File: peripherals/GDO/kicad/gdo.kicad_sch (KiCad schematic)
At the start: 11 parts, among them J1 Conn_01x15_Pin, J2 Conn_01x02_Pin, J4 Conn_01x03_Pin, J5 Conn_01x03_Pin, J6 Conn_01x03_Pin, Q1 2N7002, Q2 AO3400A

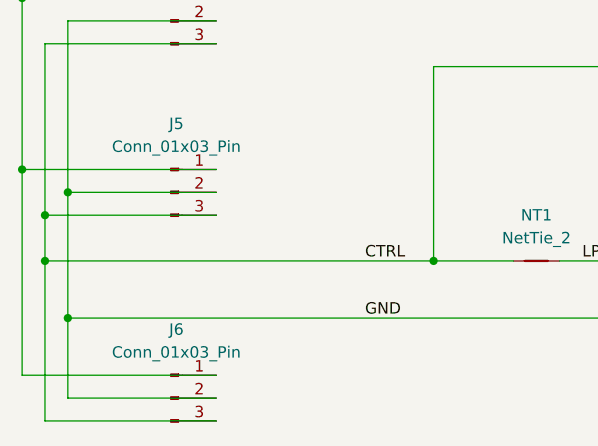
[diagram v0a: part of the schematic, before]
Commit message: Adding GDO peripheral BOM, PCBWay project, and enclosure face plate.
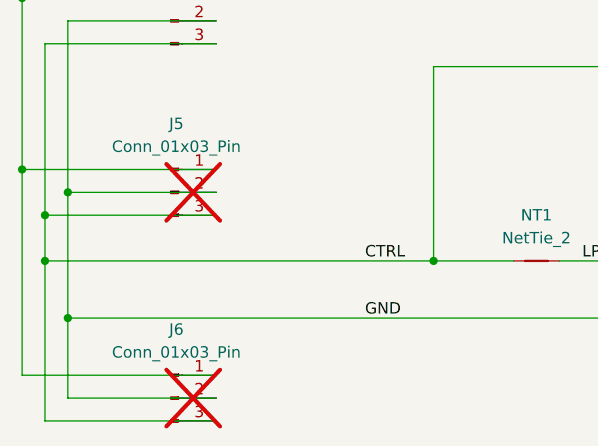
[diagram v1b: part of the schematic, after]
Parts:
- J1: Manufacturer (none) -> Sullins Connector Solutions; Mfg Part # (none) -> PREC015SBAN-M71RC; Substitution (none) -> Yes; Type (none) -> through hole
- J2: Manufacturer (none) -> Harwin Inc.; Mfg Part # (none) -> M20-9990246; Substitution (none) -> Yes; Type (none) -> through hole
- J4: Manufacturer (none) -> JST; Mfg Part # (none) -> B3B-XH-A; Substitution (none) -> No; Type (none) -> through hole
- J5, J6: Manufacturer (none) -> JST; Mfg Part # (none) -> B3B-XH-A; Substitution (none) -> No; Type (none) -> through hole; now not fitted
- Q1: Manufacturer (none) -> Diotec Semiconductor; Mfg Part # (none) -> 2N7002; Package (none) -> SOT-23; Substitution (none) -> Yes; Type (none) -> SMD
- Q2: Manufacturer (none) -> Alpha & Omega Semiconductor Inc.; Mfg Part # (none) -> AO3400A; Package (none) -> SOT-23; Substitution (none) -> Yes; Type (none) -> SMD
- R1, R2, R3: Package (none) -> 0805; Substitution (none) -> Yes; Type (none) -> SMD
